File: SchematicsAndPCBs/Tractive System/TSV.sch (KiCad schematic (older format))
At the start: 22 parts, among them K1 SPST-NO (Precharge), K2 SPST-NO (AIR), K3 SPST-NO (AIR), K4 SPST-NC (Discharge), K5 SPDT (Precharge Control), SW1 HVD, SW2 SMD, SW3 SMD, U1 TSAL_ISOLATION, U2 TSAL, U3 RinehartPM100DX, U4 Emrax228HV_Motor, U5 TSMP, U6 IMD

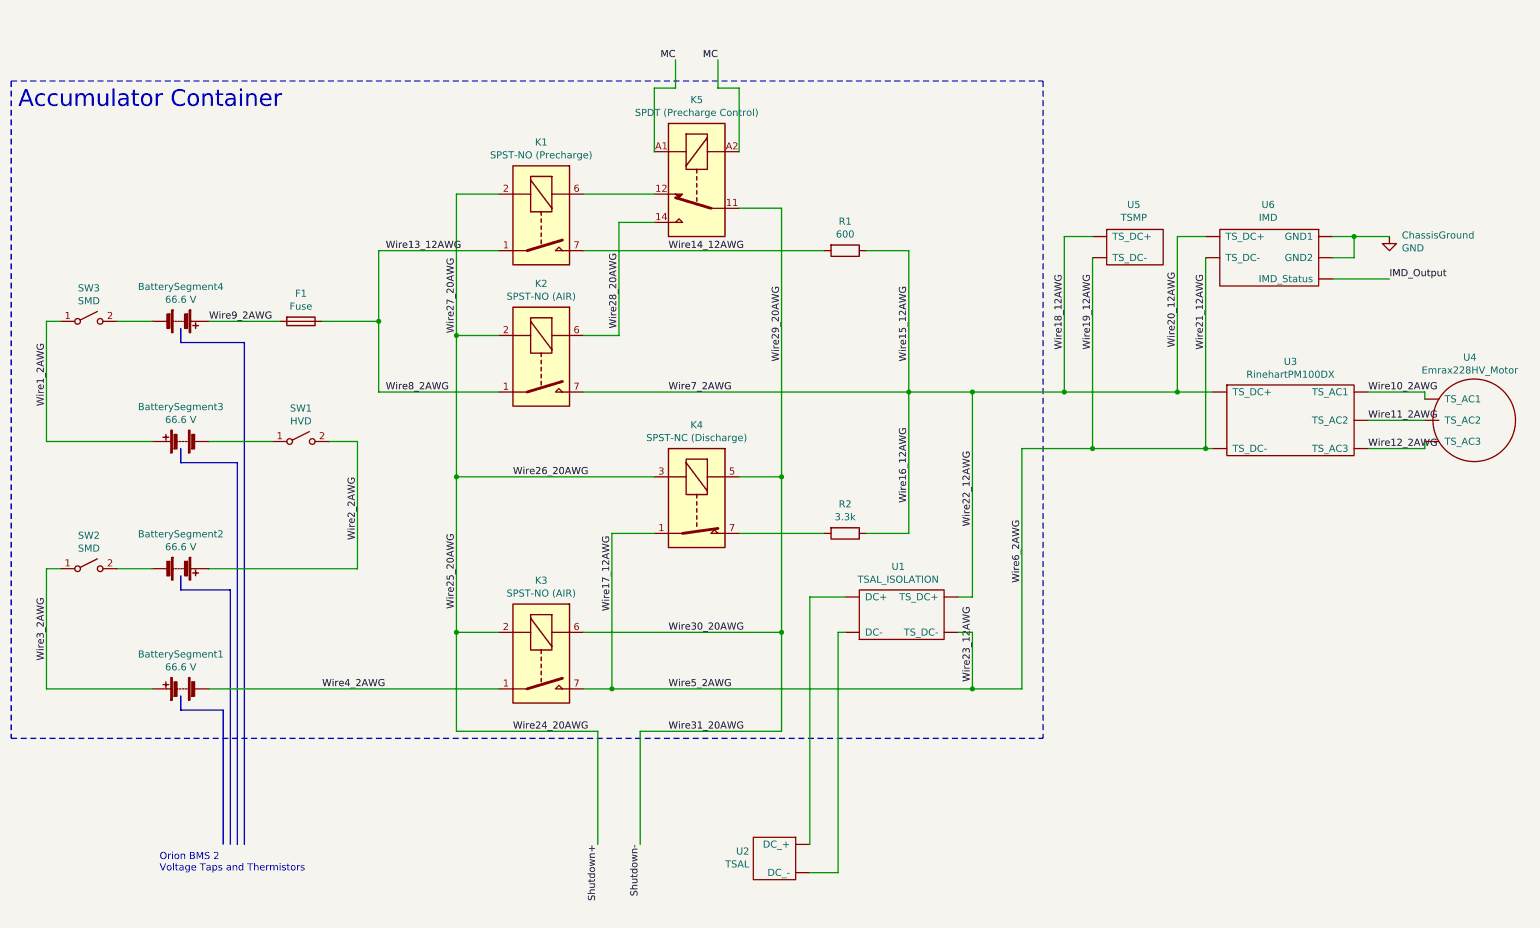
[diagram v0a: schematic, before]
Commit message: Updating TSV Schematic
-Added new TSMP/IMD branch
-Made plugs more clear
-Relabeled wires
-General cleanup
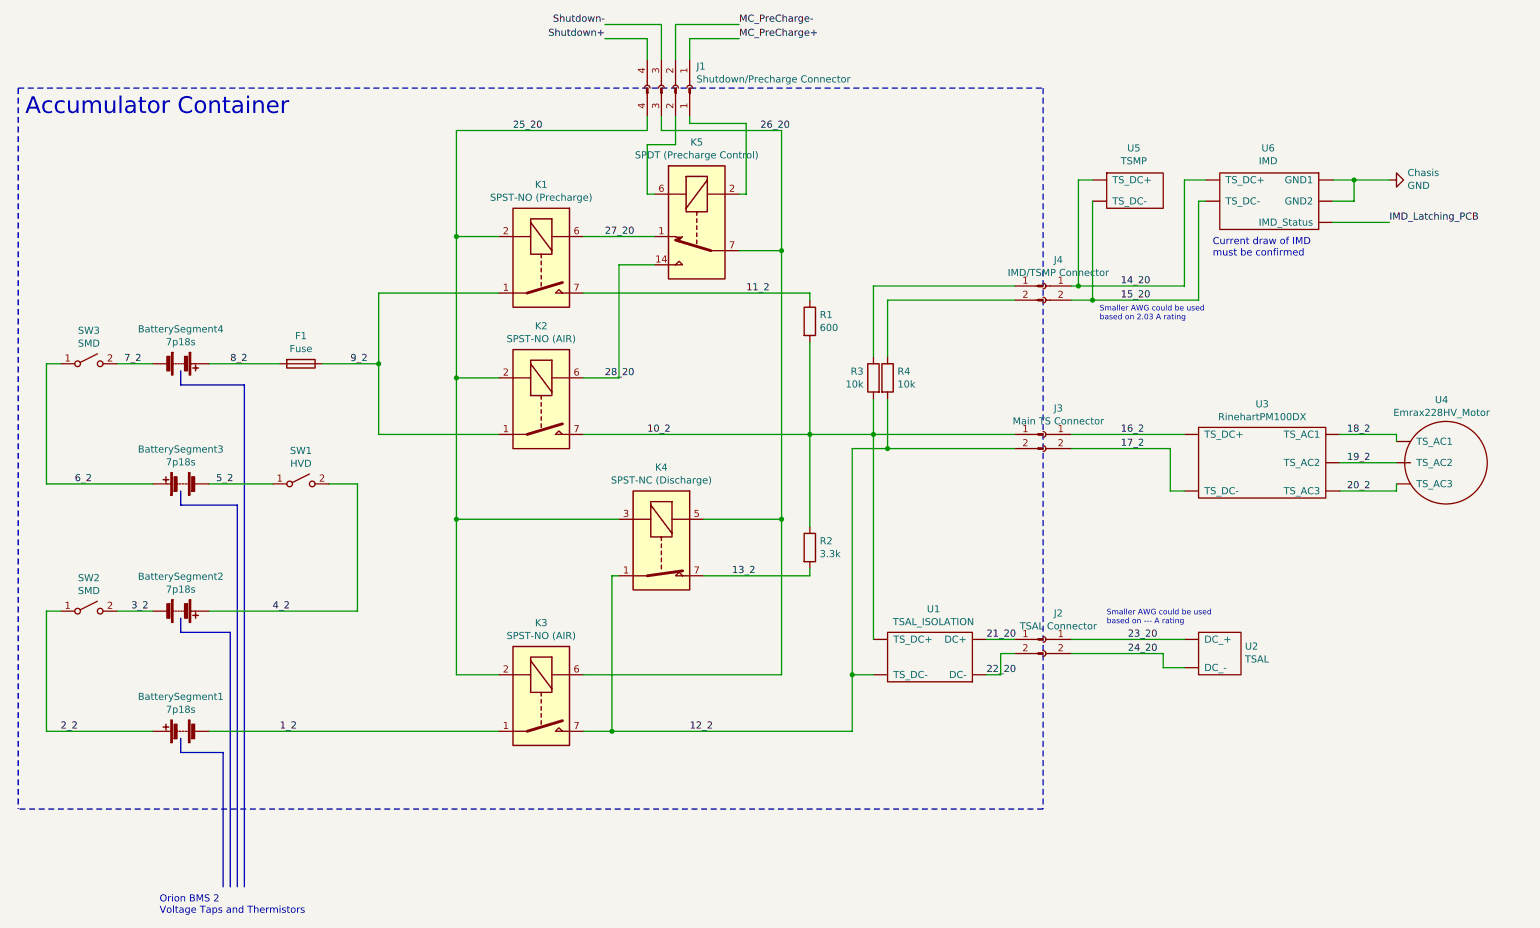
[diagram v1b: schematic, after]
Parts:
- removed ChassisGround: GND, symbol power:GND
- removed K5: SPDT (Precharge Control), Relay_THT:Relay_SPDT_Schrack-RT1-16A-FormC_RM5mm, symbol Relay:RT314A03
- added Chasis: GND, symbol power:GND
- added J1: Shutdown/Precharge Connector, symbol Connector:Conn_01x04_Female
- added J2: TSAL Connector, symbol Connector:Conn_01x02_Female
- added J3: Main TS Connector, symbol Connector:Conn_01x02_Female
- added J4: IMD/TSMP Connector, symbol Connector:Conn_01x02_Female
- added J? (x3): Conn_01x02_Male, symbol Connector:Conn_01x02_Male
- added J?: Conn_01x04_Male, symbol Connector:Conn_01x04_Male
- added K5: SPDT (Precharge Control), Relay_THT:Relay_StandexMeder_DIP_LowProfile, symbol Relay:DIPxx-1Cxx-51x
- added R3, R4: 10k, symbol Device:R
- BatterySegment1, BatterySegment2, BatterySegment3, BatterySegment4: value 66.6 V -> 7p18s
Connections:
- net Wire11_2AWG is gone; now on net 20_2: U3.~ (TS_DC-), U4.~ (TS_AC3)
- net Wire12_2AWG is gone; now on net 20_2: U3.~ (TS_DC-), U4.~ (TS_AC3)
- net GND: now also Chasis.1 (GND)
- net Shutdown+: now also J1.4 (Pin_4); no longer K1.2, K2.2, K3.2, K4.3
- net Shutdown-: now also J1.3 (Pin_3); no longer K3.6, K4.5
- net 5_2: now reaches BatterySegment3.2 (-), SW1.1 (A)
- net 22_20: now reaches U1.~ (TS_DC-)
- net 22_20: now also J?.2 (Pin_2); no longer U2.~ (DC_-)
- net 24_20: now reaches U2.~ (DC_-)
- net 24_20: now also J2.2 (Pin_2); no longer U1.~ (TS_DC-)
- net 3_2: now reaches BatterySegment2.2 (-), SW2.2 (B)
- net 7_2: now reaches BatterySegment4.2 (-), SW3.2 (B)
- net 13_2: now reaches K4.7, R2.2
- net 27_20: now reaches K1.6
- net 27_20: now also K5.1
- net IMD_Output renamed IMD_Latching_PCB
- net Wire10_2AWG renamed 20_2
- net Wire13_12AWG renamed 9_2
- net Wire14_12AWG renamed 11_2
- net 11_2: now also R1.1; no longer R1.2
- removed net Wire15_12AWG: K2.7, K2.8, R1.1, R2.1, U1.~ (TS_DC-), U3.~ (TS_DC-), U5.~ (TS_DC-), U6.~ (TS_DC-)
- removed net Wire17_12AWG: K3.7, K3.8, K4.1, U1.~ (TS_DC-), U3.~ (TS_DC-), U5.~ (TS_DC-), U6.~ (TS_DC-)
- net Wire1_2AWG renamed 6_2
- net Wire28_20AWG renamed 28_20
- net 28_20: now also K5.14
- net Wire2_2AWG renamed 4_2
- net Wire3_2AWG renamed 2_2
- net Wire4_2AWG renamed 1_2
- net Wire9_2AWG renamed 8_2
- new net: J?.1 (Pin_1), R3.1
- new net: J?.2 (Pin_2), R4.1
- new net: J?.1 (Pin_1), K5.2
- new net: J?.2 (Pin_2), K5.6
- new net 10_2: J?.1 (Pin_1), K2.7, K2.8, R1.2, R2.1, R3.2, U1.~ (TS_DC-)
- new net 12_2: J?.2 (Pin_2), K3.7, K3.8, K4.1, R4.2, U1.~ (TS_DC-)
- new net 14_20: J4.1 (Pin_1), U5.~ (TS_DC-), U6.~ (TS_DC-)
- new net 15_20: J4.2 (Pin_2), U5.~ (TS_DC-), U6.~ (TS_DC-)
- new net 16_2: J3.1 (Pin_1), U3.~ (TS_DC-)
- new net 17_2: J3.2 (Pin_2), U3.~ (TS_DC-)
- new net 18_2: U3.~ (TS_DC-), U4.~ (TS_AC3)
- new net 19_2: U3.~ (TS_DC-), U4.~ (TS_AC3)
- new net 21_20: J?.1 (Pin_1), U1.~ (TS_DC-)
- new net 23_20: J2.1 (Pin_1), U2.~ (DC_-)
- new net 25_20: J?.4 (Pin_4), K1.2, K2.2, K3.2, K4.3
- new net 26_20: J?.3 (Pin_3), K3.6, K4.5, K5.7, K5.8
- new net MC_PreCharge+: J1.1 (Pin_1)
- new net MC_PreCharge-: J1.2 (Pin_2)
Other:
- note added: "Current draw of IMD\nmust be confirmed"
- note added: "Smaller AWG could be used\nbased on --- A rating"
- note added: "Smaller AWG could be used\nbased on 2.03 A rating"
- moved on the sheet: BatterySegment1, BatterySegment2, BatterySegment3, BatterySegment4, F1, K1, K2, K3, K4, SW1, SW2, SW3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

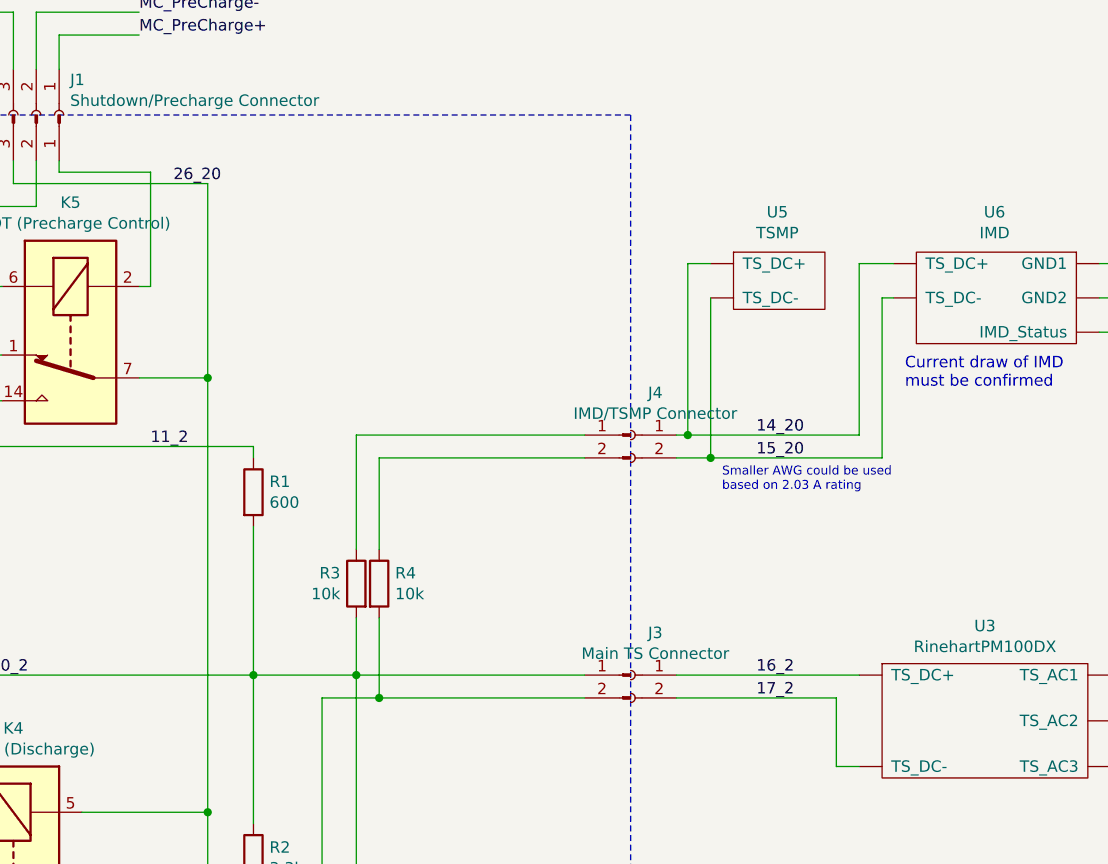
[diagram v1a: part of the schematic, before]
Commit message: IMD/TSMP Seperation
Can be in the same plug, but need to be seperated electrically due to the resistor requirement for the TSMPs
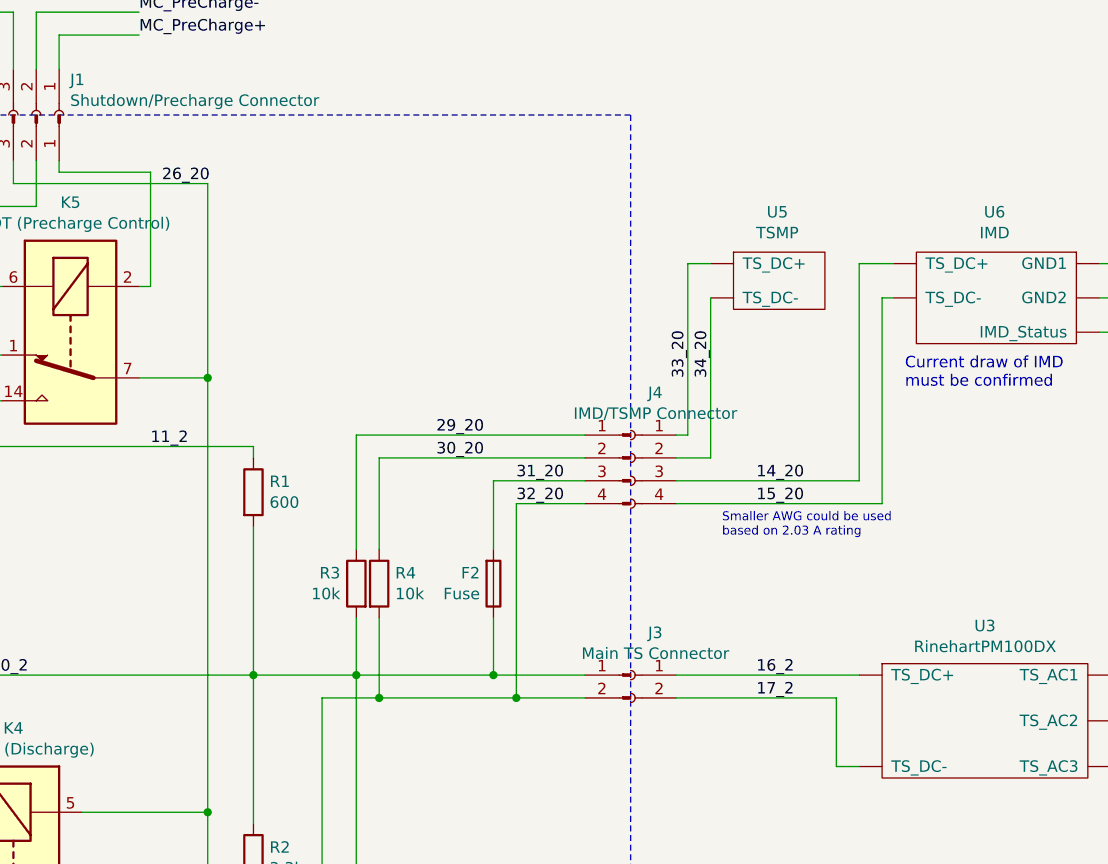
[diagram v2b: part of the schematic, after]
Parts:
- removed J4: IMD/TSMP Connector, symbol Connector:Conn_01x02_Female
- removed J?: Conn_01x02_Male, symbol Connector:Conn_01x02_Male
- added F2: Fuse, symbol Device:Fuse
- added J4: IMD/TSMP Connector, symbol Connector:Conn_01x04_Female
- added J?: Conn_01x04_Male, symbol Connector:Conn_01x04_Male
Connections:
- net 10_2: now also F2.1
- net 12_2: now also J?.4 (Pin_4)
- net 14_20: now also J4.3 (Pin_3); no longer U5.~ (TS_DC-)
- net 15_20: now also J4.4 (Pin_4); no longer U5.~ (TS_DC-)
- net 29_20: now reaches R3.1
- net 29_20: now also J?.1 (Pin_1)
- net 30_20: now reaches R4.1
- net 30_20: now also J?.2 (Pin_2)
- new net 31_20: F2.2, J?.3 (Pin_3)
- new net 33_20: J4.1 (Pin_1), U5.~ (TS_DC-)
- new net 34_20: J4.2 (Pin_2), U5.~ (TS_DC-)
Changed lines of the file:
@@
-$EndComp
-$Comp
-L Connector:Conn_01x02_Female J4
-U 1 1 5F1E8BB5
-P 7850 2550
-F 0 "J4" H 7742 2735 50  0000 C CNN
-F 1 "IMD/TSMP Connector" H 7742 2644 50  0000 C CNN
-F 2 "" H 7850 2550 50  0001 C CNN
-F 3 "~" H 7850 2550 50  0001 C CNN
-	1    7850 2550
-	-1   0    0    -1
 $EndComp
 $Comp
@@
 F 3 "~" H 7850 3600 50  0001 C CNN
 	1    7850 3600
-	-1   0    0    -1
-$EndComp
-$Comp
-L Connector:Conn_01x02_Male J?
-U 1 1 5F1F04A4
-P 7850 2550
-F 0 "J?" H 7822 2524 50  0001 R CNN
-F 1 "Conn_01x02_Male" H 7822 2478 50  0001 R CNN
-F 2 "" H 7850 2550 50  0001 C CNN
-F 3 "~" H 7850 2550 50  0001 C CNN
-	1    7850 2550
 	-1   0    0    -1
 $EndComp
@@
 	6500 5300 6500 5700
 Wire Wire Line
-	7650 3600 6650 3600
+	7650 3600 7250 3600
 Connection ~ 6650 3600
 Wire Wire Line
@@
 	8200 2650 8050 2650
 Wire Wire Line
-	8100 2550 8850 2550
-Wire Wire Line
-	8850 2550 8850 1800
-Wire Wire Line
 	8850 1800 9000 1800
-Connection ~ 8100 2550
 Wire Wire Line
 	9000 1950 8950 1950
-Wire Wire Line
-	8950 1950 8950 2650
-Wire Wire Line
-	8950 2650 8200 2650
-Connection ~ 8200 2650
 Text Label 2450 5700 0    50   ~ 0
 1_2
@@
 Text Label 5350 5700 0    50   ~ 0
 12_2
-Text Label 8400 2550 0    50   ~ 0
+Text Label 8400 2750 0    50   ~ 0
 14_20
-Text Label 8400 2650 0    50   ~ 0
+Text Label 8400 2850 0    50   ~ 0
 15_20
 Text Label 8400 3600 0    50   ~ 0
@@
 Text Label 4100 1450 0    50   ~ 0
 25_20
-Text Label 5850 1450 0    50   ~ 0
+Text Label 5800 1450 0    50   ~ 0
 26_20
 Text Label 5650 4600 0    50   ~ 0
@@
 Wire Wire Line
 	8850 3600 8050 3600
-Text Notes 8250 2800 0    39   ~ 0
+Text Notes 8250 3000 0    39   ~ 0
 Smaller AWG could be used\nbased on 2.03 A rating
 Text Notes 8300 4950 0    39   ~ 0
@@
 Connection ~ 6750 3700
 Wire Wire Line
-	6750 3700 7650 3700
+	6750 3700 7350 3700
 Wire Wire Line
 	6650 3600 6650 3350
+$Comp
+L Device:Fuse F2
+U 1 1 5F14BDC4
+P 7250 3200
+F 0 "F2" H 7191 3154 50  0000 R CNN
+F 1 "Fuse" H 7191 3245 50  0000 R CNN
+F 2 "" V 7180 3200 50  0001 C CNN
+F 3 "~" H 7250 3200 50  0001 C CNN
+	1    7250 3200
+	1    0    0    1
+$EndComp
+Wire Wire Line
+	7250 3350 7250 3600
+Connection ~ 7250 3600
+Wire Wire Line
+	7250 3600 6650 3600
+$Comp
+L Connector:Conn_01x04_Female J4
+U 1 1 5F1518CD
+P 7850 2650
+F 0 "J4" H 7742 2935 50  0000 C CNN
+F 1 "IMD/TSMP Connector" H 7742 2844 50  0000 C CNN
+F 2 "" H 7850 2650 50  0001 C CNN
+F 3 "~" H 7850 2650 50  0001 C CNN
+	1    7850 2650
+	-1   0    0    -1
+$EndComp
+$Comp
+L Connector:Conn_01x04_Male J?
+U 1 1 5F154419
+P 7850 2650
+F 0 "J?" H 7822 2578 50  0001 R CNN
+F 1 "Conn_01x04_Male" H 7822 2533 50  0001 R CNN
+F 2 "" H 7850 2650 50  0001 C CNN
+F 3 "~" H 7850 2650 50  0001 C CNN
+	1    7850 2650
+	-1   0    0    -1
+$EndComp
+Wire Wire Line
+	7250 3050 7250 2750
+Wire Wire Line
+	7250 2750 7650 2750
+Wire Wire Line
+	7650 2850 7350 2850
+Wire Wire Line
+	7350 2850 7350 3700
+Connection ~ 7350 3700
+Wire Wire Line
+	7350 3700 7650 3700
+Wire Wire Line
+	8850 1800 8850 2750
+Wire Wire Line
+	8950 1950 8950 2850
+Wire Wire Line
+	8050 2850 8950 2850
+Wire Wire Line
+	8050 2750 8850 2750
+Text Label 7000 2550 0    50   ~ 0
+29_20
+Text Label 7000 2650 0    50   ~ 0
+30_20
+Text Label 7350 2750 0    50   ~ 0
+31_20
+Text Label 7350 2850 0    50   ~ 0
+32_20
+Text Label 8100 2300 1    50   ~ 0
+33_20
+Text Label 8200 2300 1    50   ~ 0
+34_20
 $EndSCHEMATC
